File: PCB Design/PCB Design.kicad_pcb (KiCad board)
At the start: 2 copper layers, 8 parts, among them J1 Screw_Terminal_01x02, K1 SANYOU_SRD_Form_C, Q1 BC547

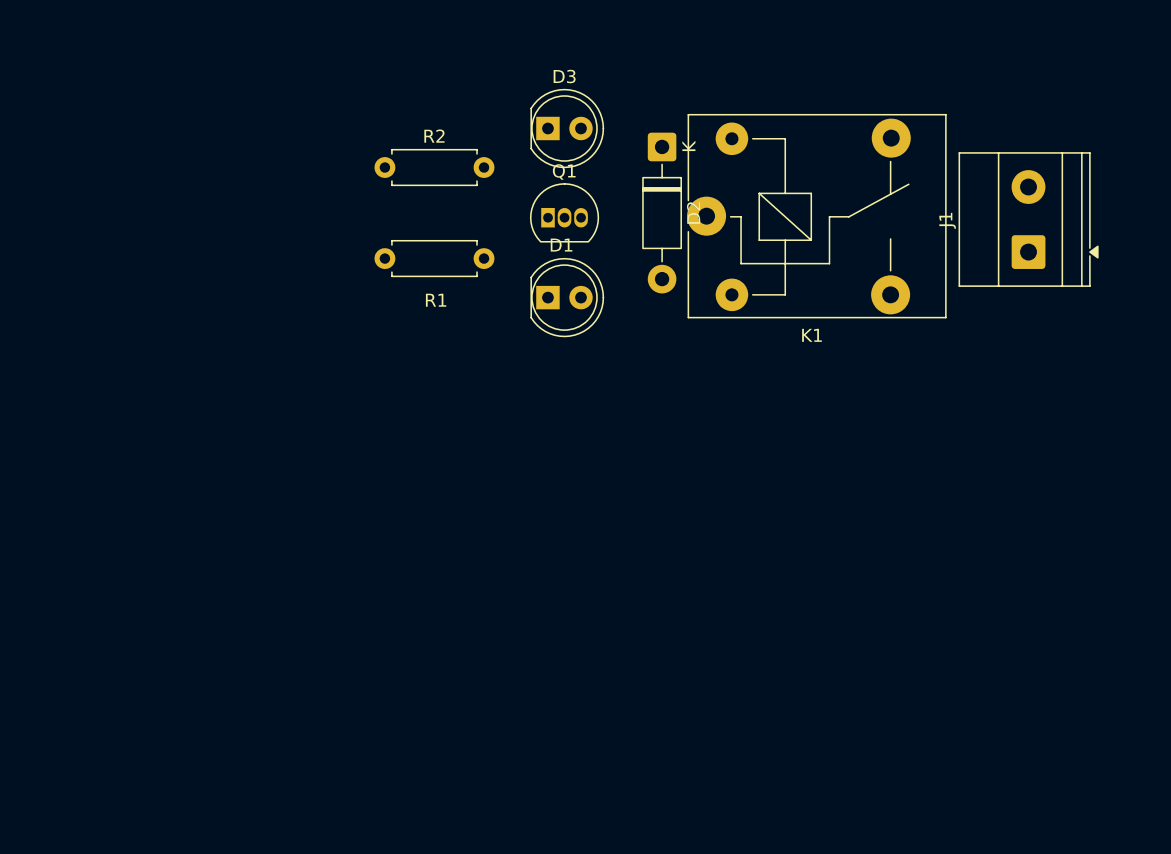
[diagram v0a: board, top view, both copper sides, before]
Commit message: Finished the first version of the PCB design. Added the footprint library table and removed the lock file.
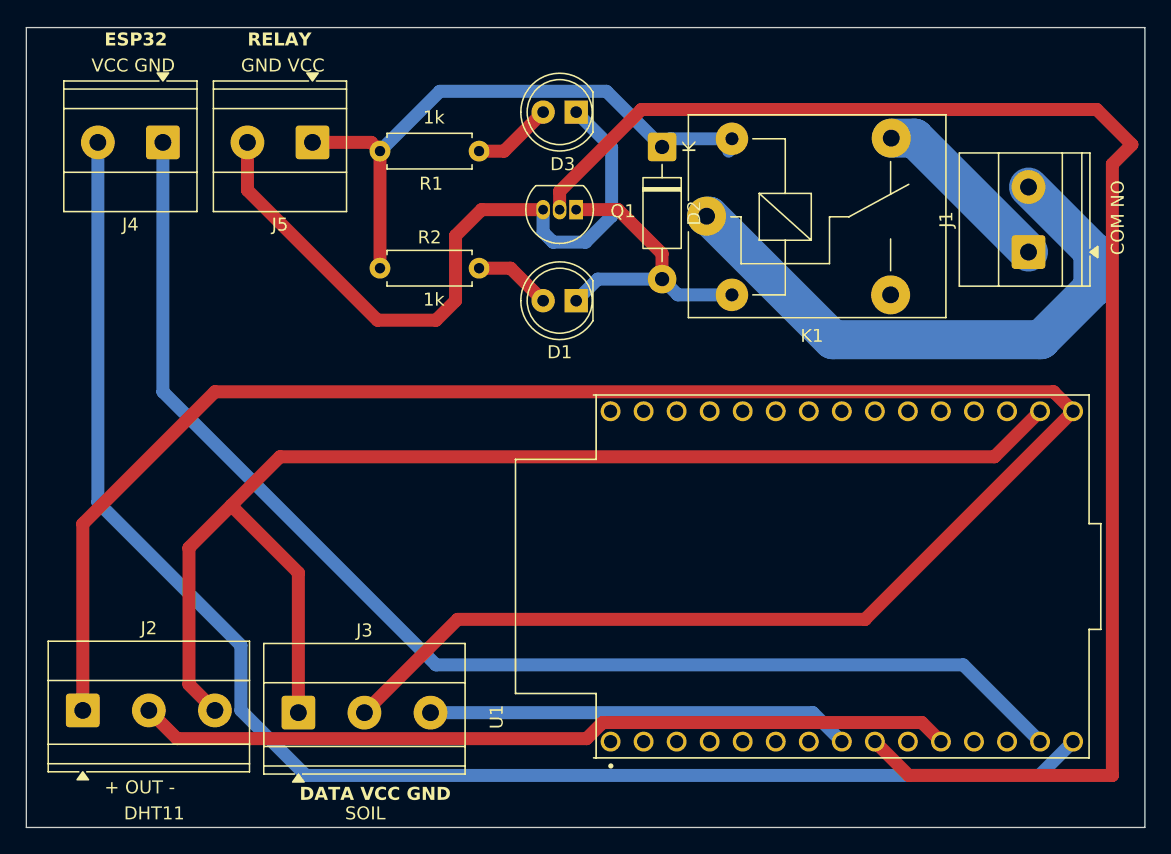
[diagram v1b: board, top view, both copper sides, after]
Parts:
- added J2: Screw_Terminal_01x03, TerminalBlock_Phoenix:TerminalBlock_Phoenix_MKDS-1,5-3-5.08_1x03_P5.08mm_Horizontal, F.Cu at (178.3, 92.5)
- added J3: Screw_Terminal_01x03, TerminalBlock_Phoenix:TerminalBlock_Phoenix_MKDS-1,5-3-5.08_1x03_P5.08mm_Horizontal, F.Cu at (194.9, 92.7)
- added J4: Screw_Terminal_01x02, TerminalBlock_Phoenix:TerminalBlock_Phoenix_MKDS-1,5-2_1x02_P5.00mm_Horizontal, F.Cu at (184.5, 48.8)
- added J5: Screw_Terminal_01x02, TerminalBlock_Phoenix:TerminalBlock_Phoenix_MKDS-1,5-2_1x02_P5.00mm_Horizontal, F.Cu at (196.0, 48.8)
- added U1: DEVKIT_V1_ESP32-WROOM-32, DEVKIT_V1_ESP32-WROOM-32:MODULE_DEVKIT_V1_ESP32-WROOM-32, F.Cu at (231.6, 82.2)
- moved D3 14.4 mm to (216.3, 46.5), turned to 180 degrees
- moved D1 13.4 mm to (216.3, 61.0), turned to 180 degrees
- moved R1 8.27 mm to (201.2, 49.5)
- moved R2 7.75 mm to (201.2, 58.5)
- moved Q1 2.25 mm to (216.3, 54.0), turned to 180 degrees
- renumbered D3 to D1, D1 to D3
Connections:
- net +5V renamed Net-(D2-K)
- Q1 pad 2: unconnected-(Q1-B-Pad2) -> Net-(Q1-B)
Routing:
- net Net-(J2-Pin_1): track 0.00 -> 159.4 mm
- net Net-(Q1-B): track 0.00 -> 117.6 mm
- net Net-(J4-Pin_2): track 0.00 -> 115.4 mm
- net Net-(J2-Pin_3): track 0.00 -> 101.2 mm
- net Net-(J4-Pin_1): track 0.00 -> 97.8 mm
- net Net-(J2-Pin_2): track 0.00 -> 62.9 mm
- net GND: track 0.00 -> 54.3 mm
- net Net-(D2-K): track 0.00 -> 46.5 mm
- net Net-(J1-Pin_2): track 0.00 -> 45.1 mm
- net Net-(J3-Pin_3): track 0.00 -> 32.5 mm
- net Net-(D1-K): track 0.00 -> 23.1 mm
- net Net-(J1-Pin_1): track 0.00 -> 14.2 mm
- net Net-(D3-A): track 0.00 -> 6.17 mm
- net Net-(D1-A): track 0.00 -> 5.96 mm
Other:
- board outline added: 86 x 61.5 mm
- board text added: "+ OUT -"
- board text added: "1k"
- board text added: "COM NO"
- board text added: "DATA VCC GND"
- board text added: "DHT11"
- board text added: "ESP32"
- board text added: "GND VCC"
- board text added: "RELAY"
- board text added: "SOIL"
- board text added: "VCC GND"
